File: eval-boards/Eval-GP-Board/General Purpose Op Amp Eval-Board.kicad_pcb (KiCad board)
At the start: 2 copper layers, 81.3 x 53.3 mm, 68 parts, among them J2 Conn_01x03_Male, U1 ADA4522-2, U2 ADA4075-2, U3 ADA4807-2ARM

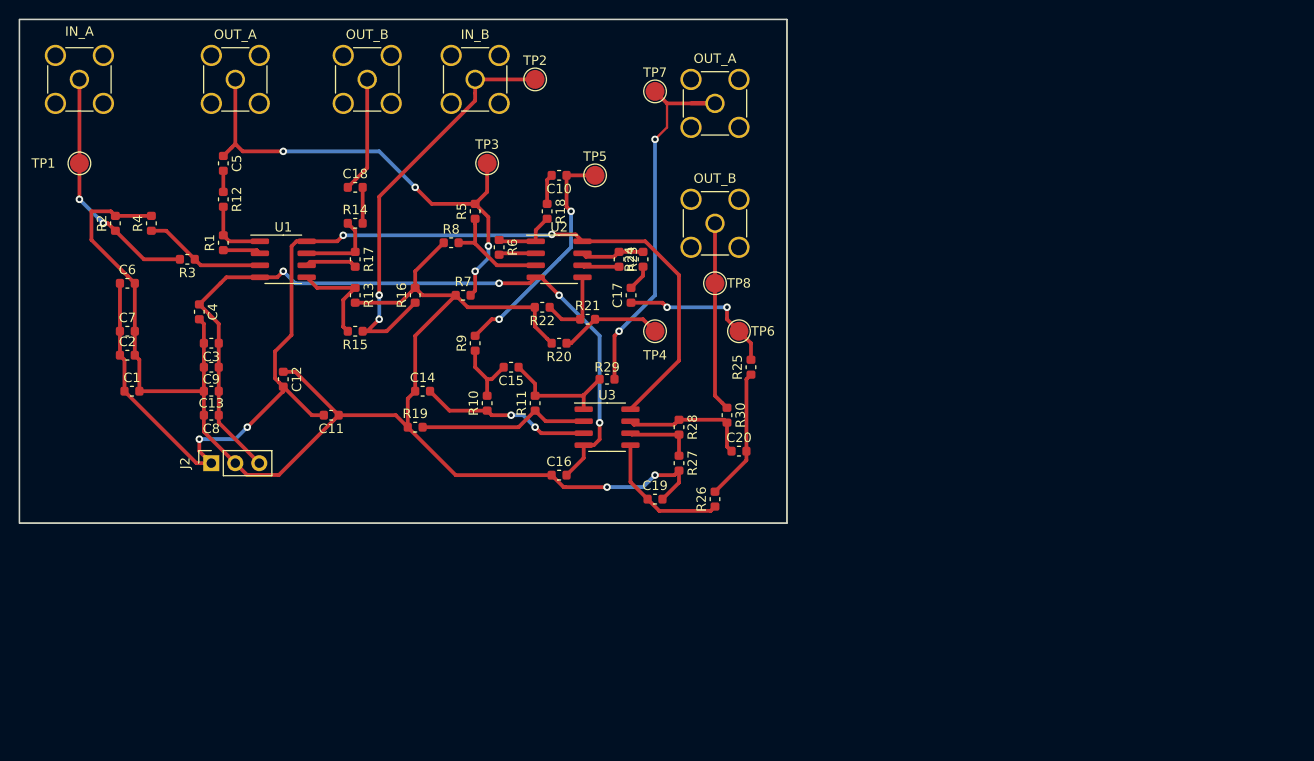
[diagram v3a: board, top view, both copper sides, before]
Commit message: 双通道通用精密放大器PCB
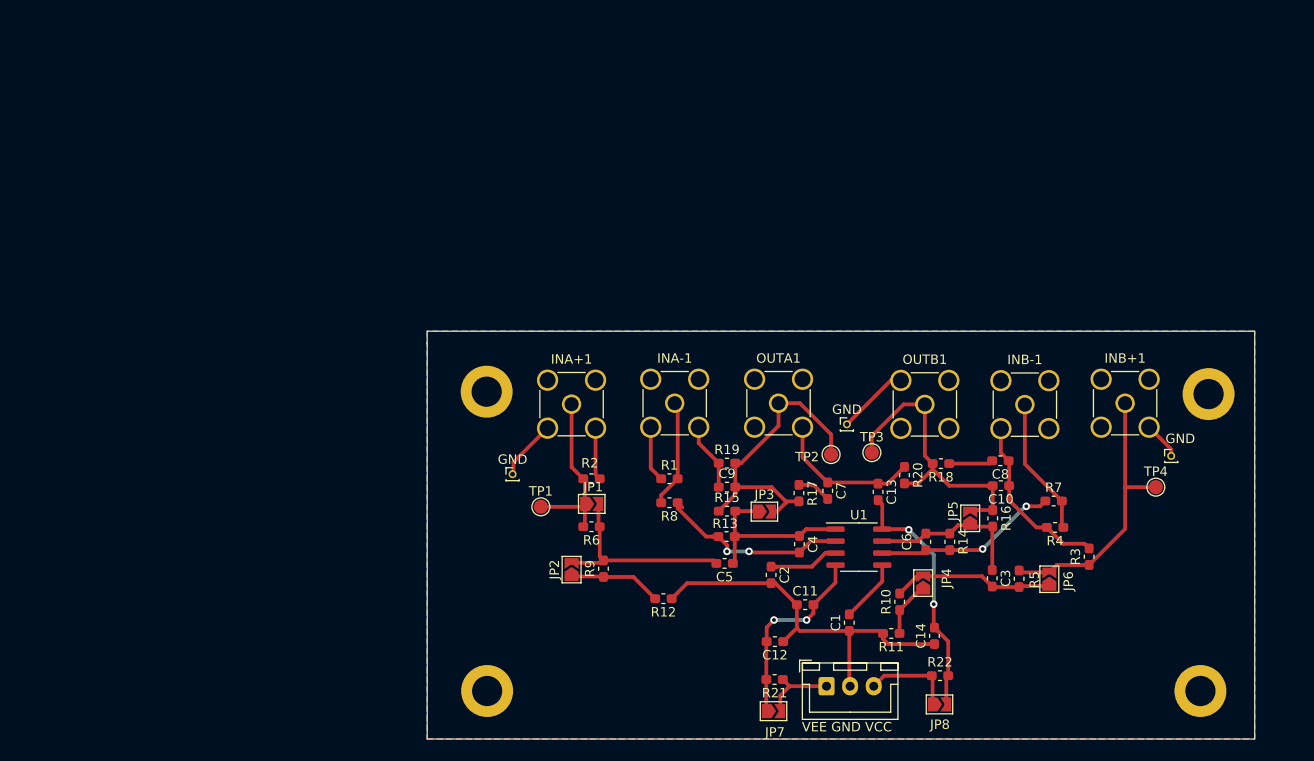
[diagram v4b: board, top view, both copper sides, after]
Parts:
- removed C15, C16, C17, C18, C19, C20: C, Capacitor_SMD:C_0603_1608Metric
- removed IN_A: IN_A, Connector_Coaxial:SMA_Amphenol_901-144_Vertical
- removed IN_B: IN_B, Connector_Coaxial:SMA_Amphenol_901-144_Vertical
- removed J2: Conn_01x03_Male, Connector_PinSocket_2.54mm:PinSocket_1x03_P2.54mm_Vertical
- removed OUT_A (x2): OUT_A, Connector_Coaxial:SMA_Amphenol_901-144_Vertical
- removed OUT_B (x2): OUT_B, Connector_Coaxial:SMA_Amphenol_901-144_Vertical
- removed R23, R24, R25, R26, R27, R28, R29, R30: R, Resistor_SMD:R_0603_1608Metric
- removed TP5: TP5, TestPoint:TestPoint_Pad_D2.0mm
- removed TP6: TP6, TestPoint:TestPoint_Pad_D2.0mm
- removed TP7: TP7, TestPoint:TestPoint_Pad_D2.0mm
- removed TP8: TP8, TestPoint:TestPoint_Pad_D2.0mm
- removed U2: ADA4075-2, Package_SO:SOIC-8_3.9x4.9mm_P1.27mm
- removed U3: ADA4807-2ARM, Package_SO:SOIC-8_3.9x4.9mm_P1.27mm
- added GND: PinHeader_1x01_P1.00mm_Vertical, Connector_PinHeader_1.00mm:PinHeader_1x01_P1.00mm_Vertical, F.Cu at (167.7, 98.3)
- added GND: PinHeader_1x01_P1.00mm_Vertical, Connector_PinHeader_1.00mm:PinHeader_1x01_P1.00mm_Vertical, F.Cu at (133.3, 94.9)
- added GND: PinHeader_1x01_P1.00mm_Vertical, Connector_PinHeader_1.00mm:PinHeader_1x01_P1.00mm_Vertical, F.Cu at (97.9, 100.2)
- added INA+1: Conn_Coaxial, Connector_Coaxial:SMA_Amphenol_132134-11_Vertical, F.Cu at (104.2, 92.8)
- added INA-1: Conn_Coaxial, Connector_Coaxial:SMA_Amphenol_132134-11_Vertical, F.Cu at (115.1, 92.7)
- added INB+1: Conn_Coaxial, Connector_Coaxial:SMA_Amphenol_132134-11_Vertical, F.Cu at (162.8, 92.7)
- added INB-1: Conn_Coaxial, Connector_Coaxial:SMA_Amphenol_132134-11_Vertical, F.Cu at (152.2, 92.9)
- added JP1: SolderJumper-2_P1.3mm_Open_TrianglePad1.0x1.5mm, Jumper:SolderJumper-2_P1.3mm_Open_TrianglePad1.0x1.5mm, F.Cu at (106.3, 103.4)
- added JP2: SolderJumper-2_P1.3mm_Open_TrianglePad1.0x1.5mm, Jumper:SolderJumper-2_P1.3mm_Open_TrianglePad1.0x1.5mm, F.Cu at (104.2, 110.3)
- added JP3: SolderJumper-2_P1.3mm_Open_TrianglePad1.0x1.5mm, Jumper:SolderJumper-2_P1.3mm_Open_TrianglePad1.0x1.5mm, F.Cu at (124.6, 104.2)
- added JP4: SolderJumper-2_P1.3mm_Open_TrianglePad1.0x1.5mm, Jumper:SolderJumper-2_P1.3mm_Open_TrianglePad1.0x1.5mm, F.Cu at (141.4, 111.8)
- added JP5: SolderJumper-2_P1.3mm_Open_TrianglePad1.0x1.5mm, Jumper:SolderJumper-2_P1.3mm_Open_TrianglePad1.0x1.5mm, F.Cu at (146.4, 104.9)
- added JP6: SolderJumper-2_P1.3mm_Open_TrianglePad1.0x1.5mm, Jumper:SolderJumper-2_P1.3mm_Open_TrianglePad1.0x1.5mm, F.Cu at (154.8, 111.4)
- added JP7: SolderJumper-2_P1.3mm_Open_TrianglePad1.0x1.5mm, Jumper:SolderJumper-2_P1.3mm_Open_TrianglePad1.0x1.5mm, F.Cu at (125.6, 125.3)
- added JP8: SolderJumper-2_P1.3mm_Open_TrianglePad1.0x1.5mm, Jumper:SolderJumper-2_P1.3mm_Open_TrianglePad1.0x1.5mm, F.Cu at (143.2, 124.6)
- added OUTA1: Conn_Coaxial, Connector_Coaxial:SMA_Amphenol_132134-11_Vertical, F.Cu at (126.1, 92.7)
- added OUTB1: Conn_Coaxial, Connector_Coaxial:SMA_Amphenol_132134-11_Vertical, F.Cu at (141.6, 92.8)
- added REF**: MountingHole_3.2mm_M3_ISO14580_Pad, MountingHole:MountingHole_3.2mm_M3_ISO14580_Pad, F.Cu at (95.2, 123.2)
- added REF**: MountingHole_3.2mm_M3_ISO14580_Pad, MountingHole:MountingHole_3.2mm_M3_ISO14580_Pad, F.Cu at (170.8, 123.2)
- added REF**: MountingHole_3.2mm_M3_ISO14580_Pad, MountingHole:MountingHole_3.2mm_M3_ISO14580_Pad, F.Cu at (171.7, 91.7)
- added REF**: MountingHole_3.2mm_M3_ISO14580_Pad, MountingHole:MountingHole_3.2mm_M3_ISO14580_Pad, F.Cu at (95.2, 91.5)
- added VEE GND VCC: Conn_01x03_Male, Connector_JST:JST_XH_B3B-XH-A_1x03_P2.50mm_Vertical, F.Cu at (131.2, 122.7)
- C1, C3: value 0.1u -> C; footprint Capacitor_SMD:C_0603_1608Metric -> Capacitor_SMD:C_0603_1608Metric_Pad1.05x0.95mm_HandSolder
- C10, C11, C12, C13, C14, C5, C6, C7, C8, C9: footprint Capacitor_SMD:C_0603_1608Metric -> Capacitor_SMD:C_0603_1608Metric_Pad1.05x0.95mm_HandSolder
- C2, C4: value 10u -> C; footprint Capacitor_SMD:C_0603_1608Metric -> Capacitor_SMD:C_0603_1608Metric_Pad1.05x0.95mm_HandSolder
- R1, R10, R11, R12, R13, R14, R15, R16, R17, R18, R19, R2, R20, R21, R22, R3, R4, R5, R6, R7, R8, R9: footprint Resistor_SMD:R_0603_1608Metric -> Resistor_SMD:R_0603_1608Metric_Pad1.05x0.95mm_HandSolder
- TP1: value TP1 -> TestPoint_Pad_D1.5mm; footprint TestPoint:TestPoint_Pad_D2.0mm -> TestPoint:TestPoint_Pad_D1.5mm
- TP2: value TP2 -> TestPoint_Pad_D1.5mm; footprint TestPoint:TestPoint_Pad_D2.0mm -> TestPoint:TestPoint_Pad_D1.5mm
- TP3: value TP3 -> TestPoint_Pad_D1.5mm; footprint TestPoint:TestPoint_Pad_D2.0mm -> TestPoint:TestPoint_Pad_D1.5mm
- TP4: value TP4 -> TestPoint_Pad_D1.5mm; footprint TestPoint:TestPoint_Pad_D2.0mm -> TestPoint:TestPoint_Pad_D1.5mm
- U1: value ADA4522-2 -> ADA4075-2
- moved R4 101.0 mm to (155.4, 105.9), turned to 180 degrees
- moved R3 100.6 mm to (159.0, 109.0), turned to 90 degrees
- moved C6 88.9 mm to (141.7, 107.4), turned to 270 degrees
- moved C3 86.4 mm to (148.7, 111.3), turned to 270 degrees
- moved C8 83.7 mm to (149.6, 98.8)
- moved C1 79.8 mm to (133.6, 116.0), turned to 90 degrees
- moved C7 76.1 mm to (131.3, 102.0), turned to 270 degrees
- moved C2 72.0 mm to (125.3, 110.9), turned to 270 degrees
- moved R14 71.4 mm to (144.2, 107.4), turned to 270 degrees
- moved C13 71.4 mm to (136.7, 102.1), turned to 270 degrees
- moved R5 69.5 mm to (151.6, 111.3)
- moved U1 68.2 mm to (134.6, 108.0)
- moved C4 68.2 mm to (128.3, 107.6)
- moved C5 67.9 mm to (120.4, 109.7), turned to 180 degrees
- moved R7 66.2 mm to (155.2, 103.1)
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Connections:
- C1 pad 1: /VCC -> GND
- C1 pad 2: GND -> Net-(C1-Pad2)
- C10 pad 1: /High gain amplifier/OUT_A -> GND
- C11 pad 2: /VCC -> Net-(C11-Pad2)
- C12 pad 2: /VCC -> Net-(C11-Pad2)
- C13 pad 2: /VEE -> Net-(C13-Pad2)
- C14 pad 2: Net-(C14-Pad2) -> Net-(C13-Pad2)
- C2 pad 1: /VCC -> Net-(C2-Pad1)
- C3 pad 1: /VEE -> Net-(C3-Pad1)
- C3 pad 2: GND -> Net-(C3-Pad2)
- C4 pad 1: /VEE -> Net-(C4-Pad1)
- C4 pad 2: GND -> Net-(C4-Pad2)
- C5 pad 1: /Low noise amplifier/OUT_A -> Net-(C4-Pad1)
- C6 pad 1: /VCC -> Net-(C3-Pad1)
- C6 pad 2: GND -> Net-(C6-Pad2)
- C7 pad 1: /VCC -> GND
- C7 pad 2: GND -> Net-(C7-Pad2)
- C8 pad 1: /VEE -> GND
- C8 pad 2: GND -> Net-(C8-Pad2)
- C9 pad 1: /VEE -> GND
- C9 pad 2: GND -> Net-(C9-Pad2)
- R1 pad 1: Net-(R1-Pad1) -> GND
- R1 pad 2: Net-(R1-Pad2) -> Net-(INA-1-Pad1)
- R10 pad 1: Net-(C14-Pad2) -> Net-(R10-Pad1)
- R10 pad 2: Net-(C15-Pad2) -> Net-(C3-Pad2)
- R11 pad 1: Net-(R11-Pad1) -> Net-(R10-Pad1)
- R11 pad 2: Net-(C15-Pad1) -> GND
- R12 pad 1: Net-(C5-Pad2) -> GND
- R12 pad 2: Net-(R1-Pad2) -> Net-(R12-Pad2)
- R13 pad 1: Net-(R13-Pad1) -> Net-(C4-Pad1)
- R13 pad 2: GND -> Net-(C4-Pad2)
- R14 pad 1: Net-(R14-Pad1) -> Net-(C3-Pad1)
- R14 pad 2: Net-(C18-Pad2) -> Net-(C6-Pad2)
- R15 pad 1: /Low noise amplifier/signal_in_B -> Net-(C9-Pad2)
- R15 pad 2: Net-(R13-Pad1) -> Net-(C4-Pad1)
- R16 pad 1: /Low noise amplifier/signal_in_B -> Net-(C10-Pad2)
- R16 pad 2: GND -> Net-(C3-Pad1)
- R17 pad 1: Net-(R14-Pad1) -> Net-(C7-Pad2)
- R17 pad 2: Net-(R17-Pad2) -> Net-(C9-Pad2)
- R18 pad 1: Net-(C10-Pad2) -> Net-(C8-Pad2)
- R18 pad 2: Net-(R18-Pad2) -> Net-(C10-Pad2)
- R19 pad 2: Net-(R11-Pad1) -> Net-(C9-Pad2)
- R2 pad 1: /Low noise amplifier/signal_in_A -> GND
- R2 pad 2: GND -> Net-(INA+1-Pad1)
- R20 pad 1: Net-(J14-Pad1) -> GND
- R20 pad 2: GND -> Net-(C10-Pad2)
- R21 pad 1: Net-(R21-Pad1) -> /VEE
- R21 pad 2: Net-(J14-Pad1) -> Net-(C11-Pad2)
- R22 pad 1: Net-(R21-Pad1) -> /VCC
- R22 pad 2: GND -> Net-(C13-Pad2)
- R3 pad 1: Net-(R3-Pad1) -> Net-(INB+1-Pad1)
- R3 pad 2: /Low noise amplifier/signal_in_A -> GND
- R4 pad 1: Net-(R3-Pad1) -> Net-(INB-1-Pad1)
- R5 pad 1: Net-(R5-Pad1) -> Net-(C3-Pad2)
- R5 pad 2: /Low noise amplifier/OUT_A -> Net-(INB+1-Pad1)
- R6 pad 1: Net-(R18-Pad2) -> Net-(C5-Pad2)
- R6 pad 2: Net-(R6-Pad2) -> Net-(INA+1-Pad1)
- R7 pad 1: GND -> Net-(C6-Pad2)
- R7 pad 2: /Low noise amplifier/OUT_A -> Net-(INB-1-Pad1)
- R8 pad 1: GND -> Net-(C4-Pad2)
- R8 pad 2: Net-(R5-Pad1) -> Net-(INA-1-Pad1)
- R9 pad 1: Net-(C15-Pad2) -> Net-(R12-Pad2)
- R9 pad 2: /High gain amplifier/OUT_A -> Net-(C5-Pad2)
- TP1 pad 1: /Low noise amplifier/signal_in_A -> Net-(INA+1-Pad1)
- TP2 pad 1: /Low noise amplifier/signal_in_B -> Net-(C9-Pad2)
- TP3 pad 1: /Low noise amplifier/OUT_A -> Net-(C10-Pad2)
- TP4 pad 1: Net-(J14-Pad1) -> Net-(INB+1-Pad1)
- U1 pad 1: Net-(R1-Pad2) -> Net-(C4-Pad1)
- U1 pad 2: Net-(R1-Pad1) -> Net-(C4-Pad2)
- U1 pad 3: Net-(R3-Pad1) -> Net-(C2-Pad1)
- U1 pad 4: /VEE -> Net-(C11-Pad2)
- U1 pad 5: Net-(R13-Pad1) -> Net-(C1-Pad2)
- U1 pad 6: Net-(R17-Pad2) -> Net-(C6-Pad2)
- U1 pad 7: Net-(R14-Pad1) -> Net-(C3-Pad1)
- U1 pad 8: /VCC -> Net-(C13-Pad2)
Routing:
- net /VCC: track 119.7 -> 9.69 mm, vias 4 -> 0
- net /VEE: track 83.5 -> 8.05 mm, vias 4 -> 0
- net /Low noise amplifier/OUT_A: track 52.5 -> 0.00 mm, vias 4 -> 0
- net GND: track 164.1 -> 111.7 mm, vias 2 -> 0
- net /Low noise amplifier/signal_in_B: track 45.1 -> 0.00 mm, vias 2 -> 0
- net /Second order filtering/OUT_A: track 40.9 -> 0.00 mm, vias 2 -> 0
- net Net-(C9-Pad2): track 0.00 -> 32.9 mm
- net Net-(INB+1-Pad1): track 0.00 -> 29.8 mm
- net Net-(C10-Pad2): track 3.22 -> 31.7 mm
- net Net-(C13-Pad2): track 0.00 -> 26.4 mm, vias 0 -> 2
- net /Low noise amplifier/signal_in_A: track 26.0 -> 0.00 mm, vias 2 -> 0
- net /High gain amplifier/OUT_A: track 24.9 -> 0.00 mm, vias 2 -> 0
- net Net-(C4-Pad2): track 0.00 -> 20.8 mm, vias 0 -> 2
- net Net-(C11-Pad2): track 0.00 -> 20.5 mm, vias 0 -> 2
- net /Second order filtering/OUT_B: track 20.1 -> 0.00 mm
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- added copper zone on B.Cu, net GND
- added copper zone on F.Cu, net GND
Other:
- board size 81.3 x 53.3 mm -> 87.6 x 43.2 mm
